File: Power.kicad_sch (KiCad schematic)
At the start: 14 parts, among them J1 Conn_01x01, J2 Conn_01x01, J3 Conn_01x01, J4 Conn_01x01, J5 Conn_01x01, Q1 BSP89, Q2 BSP89, Q3 BSP89, Q4 BSP89, Q5 BSP89, Q6 BSP89

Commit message: Стартовый вариант
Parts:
- added C14, C15, C16, C17, C18, C19, C20, C21, C22, C23, C24, C25, C26, C27, C28, C29, C30, C31, C32, C33, C34, C35, C36, C37, C38, C39, C40, C41, C42, C43, C44, C45, C46, C47, C48: 4.7u, Capacitor_SMD:C_1206_3216Metric_Pad1.33x1.80mm_HandSolder, symbol Device:C_Small
- C3: footprint Capacitor_THT:CP_Axial_L30.0mm_D18.0mm_P35.00mm_Horizontal -> Capacitor_THT:CP_Axial_L18.0mm_D8.0mm_P25.00mm_Horizontal
- J1, J2, J3, J4, J5: footprint (none) -> Connector_My:Power_Wire
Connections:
- net A2 is gone; now on net A: J1.1 (Pin_1)
- net B2 is gone; now on net B: J2.1 (Pin_1)
- net C2 is gone; now on net C: J3.1 (Pin_1)
- net +24V: now also C14.1, C15.1, C16.1, C17.1, C18.1, C19.1, C20.1, C21.1, C22.1, C23.1, C24.1, C25.1, C26.1, C27.1, C28.1, C29.1, C30.1, C31.1, C32.1, C33.1, C34.1, C35.1, C36.1, C37.1, C38.1, C39.1, C40.1, C41.1, C42.1, C43.1, C44.1, C45.1, C46.1, C47.1, C48.1
- net GND: now also C14.2, C15.2, C16.2, C17.2, C18.2, C19.2, C20.2, C21.2, C22.2, C23.2, C24.2, C25.2, C26.2, C27.2, C28.2, C29.2, C30.2, C31.2, C32.2, C33.2, C34.2, C35.2, C36.2, C37.2, C38.2, C39.2, C40.2, C41.2, C42.2, C43.2, C44.2, C45.2, C46.2, C47.2, C48.2
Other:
- moved on the sheet: C1, C2, C3, J1, J2, J3, J4, J5, Q1, Q2, Q3, Q4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

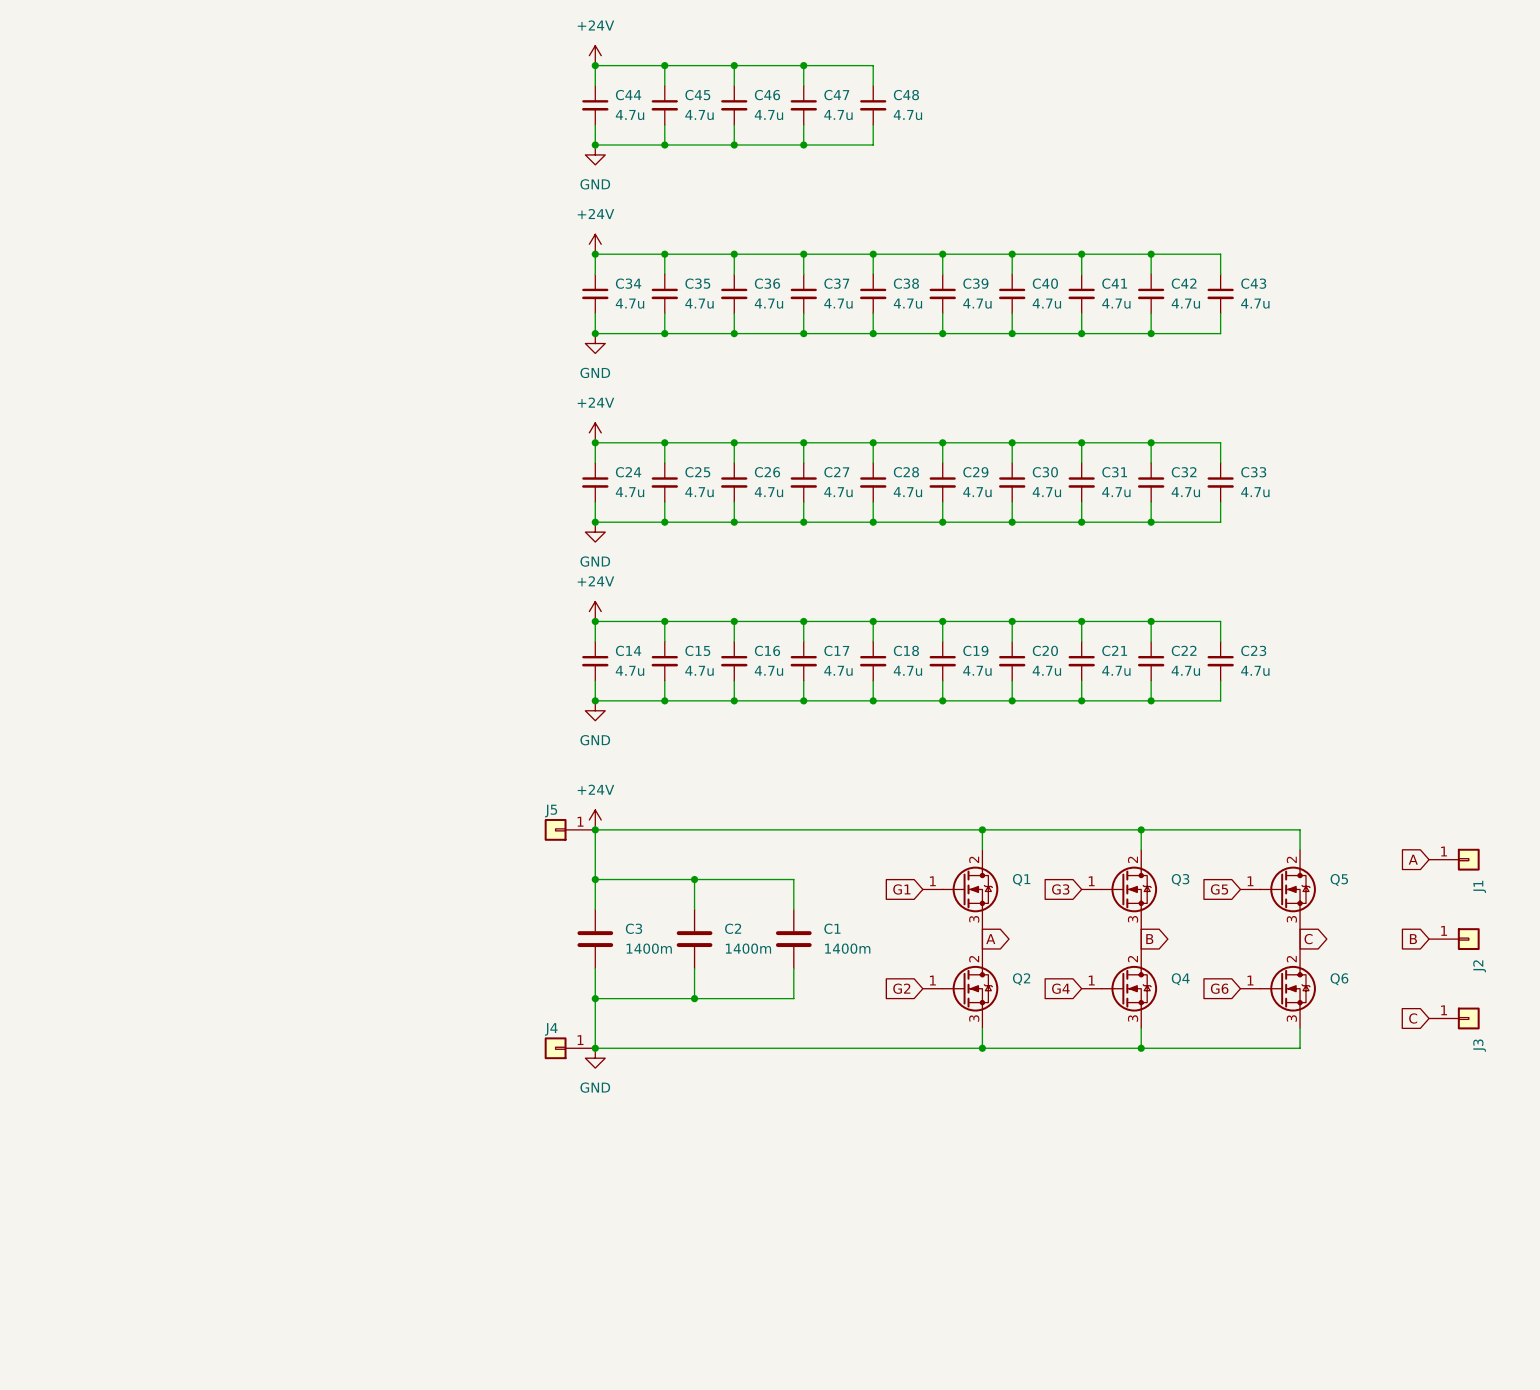
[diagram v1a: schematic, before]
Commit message: Добавил шунты
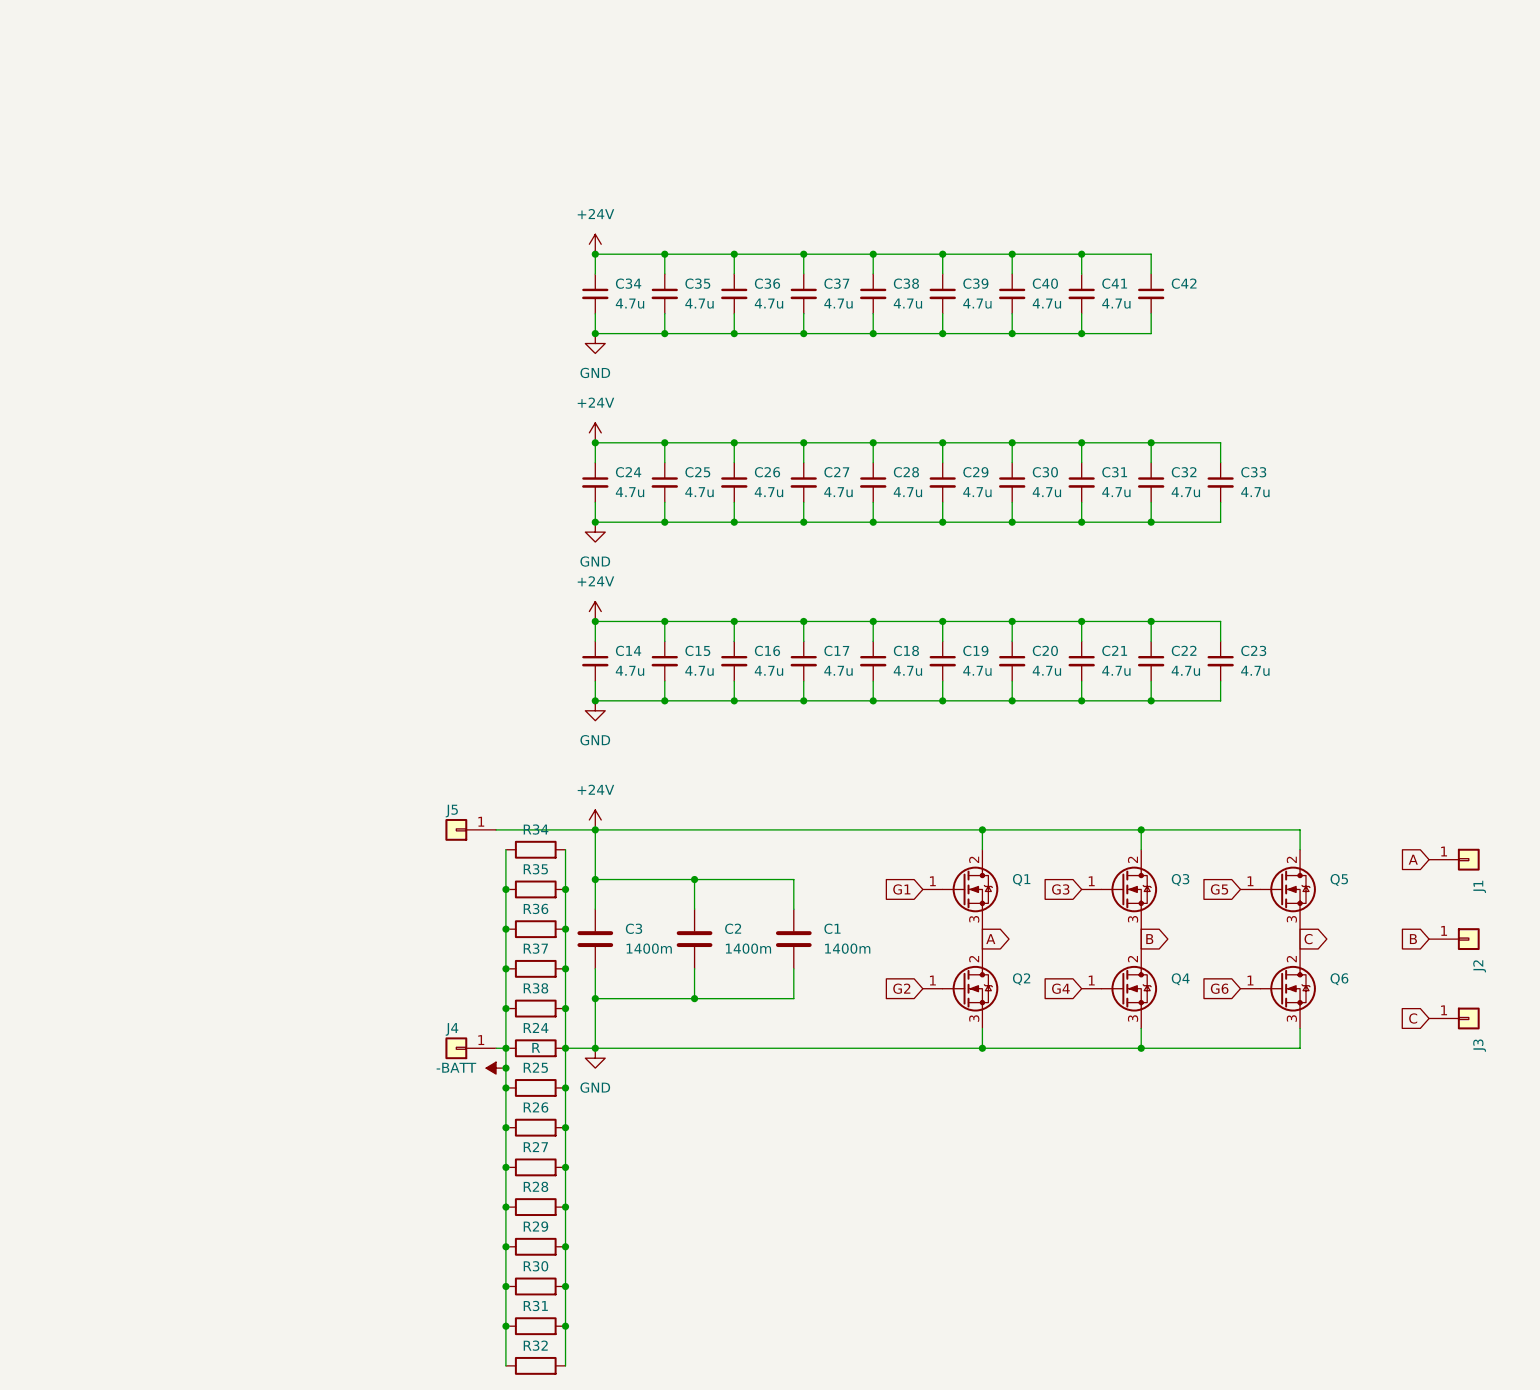
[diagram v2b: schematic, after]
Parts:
- removed C43, C44, C45, C46, C47, C48: 4.7u, Capacitor_SMD:C_1206_3216Metric_Pad1.33x1.80mm_HandSolder, symbol Device:C_Small
- added R24, R25, R26, R27, R28, R29, R30, R31, R32, R34, R35, R36, R37, R38: R, Resistor_SMD:R_2512_6332Metric_Pad1.40x3.35mm_HandSolder, symbol Device:R
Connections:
- net GND: now also R24.2, R25.2, R26.2, R27.2, R28.2, R29.2, R30.2, R31.2, R32.2, R34.2, R35.2, R36.2, R37.2, R38.2; no longer J4.1 (Pin_1)
- new net -BATT: J4.1 (Pin_1), R24.1, R25.1, R26.1, R27.1, R28.1, R29.1, R30.1, R31.1, R32.1, R34.1, R35.1, R36.1, R37.1, R38.1
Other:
- moved on the sheet: J4, J5

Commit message: Для презентации
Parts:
- removed C1: 1400m, Capacitor_THT:CP_Axial_L30.0mm_D18.0mm_P35.00mm_Horizontal, symbol Device:C
- removed R24, R25, R26, R27, R28, R29, R30, R31, R32, R35, R36, R37, R38: R, Resistor_SMD:R_2512_6332Metric_Pad1.40x3.35mm_HandSolder, symbol Device:R
- C3: footprint Capacitor_THT:CP_Axial_L18.0mm_D8.0mm_P25.00mm_Horizontal -> Capacitor_THT:CP_Axial_L30.0mm_D18.0mm_P35.00mm_Horizontal
- R34: footprint Resistor_SMD:R_2512_6332Metric_Pad1.40x3.35mm_HandSolder -> Resistor_SMD:R_Shunt_Vishay_WSR2_WSR3
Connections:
- net +24V: now also R34.1; no longer Q1.2 (D), Q3.2 (D), Q5.2 (D)
- net GND: now also J4.1 (Pin_1); no longer R34.2
- removed net -BATT: J4.1 (Pin_1), R34.1
- new net: Q1.2 (D), Q3.2 (D), Q5.2 (D), R34.2
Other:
- moved on the sheet: R34

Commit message: Стартовый вариант
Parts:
- removed C34, C35, C36, C37, C38, C39, C40, C41, C42: 4.7u, Capacitor_SMD:C_1206_3216Metric_Pad1.33x1.80mm_HandSolder, symbol Device:C_Small
- added R1: R, Shunt_My:TLRS1050, symbol Device:R
- R34: footprint Resistor_SMD:R_Shunt_Vishay_WSR2_WSR3 -> Shunt_My:TLRS1050
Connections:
- net +24V: now also R1.1
- net Shunt_2: now reaches Q1.2 (D), Q3.2 (D), Q5.2 (D), R34.2
- net Shunt_2: now also R1.2

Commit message: Стартовая версия
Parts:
- removed C22, C23, C24, C25, C26, C27, C28, C29, C30, C31, C32, C33: 4.7u, Capacitor_SMD:C_1206_3216Metric_Pad1.33x1.80mm_HandSolder, symbol Device:C_Small

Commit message: Стартовая версия
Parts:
- removed C14, C15, C16, C17, C18, C19, C20, C21: 4.7u, Capacitor_SMD:C_1206_3216Metric_Pad1.33x1.80mm_HandSolder, symbol Device:C_Small
- removed C2: 1400m, Capacitor_THT:CP_Axial_L30.0mm_D18.0mm_P35.00mm_Horizontal, symbol Device:C
- removed Q1, Q2, Q3, Q4, Q5, Q6: BSP89, Package_TO_SOT_SMD:TO-263-2, symbol Transistor_FET:BSP89
- added Q1 (x24): BSP89, Package_SON:VSONP-8-1EP_5x6_P1.27mm, symbol Transistor_FET:BSP89
- C3: footprint Capacitor_THT:CP_Axial_L30.0mm_D18.0mm_P35.00mm_Horizontal -> Capacitor_SMD:CP_Elec_10x12.5
- J4, J5: footprint Connector_My:Power_Wire -> (none)
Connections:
- net A: now also Q1.2 (D), Q1.2 (D), Q1.2 (D), Q1.2 (D), Q1.3 (S), Q1.3 (S), Q1.3 (S), Q1.3 (S)
- net B: now also Q1.2 (D), Q1.2 (D), Q1.2 (D), Q1.2 (D), Q1.3 (S), Q1.3 (S), Q1.3 (S), Q1.3 (S)
- net C: now also Q1.2 (D), Q1.2 (D), Q1.2 (D), Q1.2 (D), Q1.3 (S), Q1.3 (S), Q1.3 (S), Q1.3 (S)
- net G1: now also Q1.1 (G), Q1.1 (G), Q1.1 (G), Q1.1 (G)
- net G2: now also Q1.1 (G), Q1.1 (G), Q1.1 (G), Q1.1 (G)
- net G3: now also Q1.1 (G), Q1.1 (G), Q1.1 (G), Q1.1 (G)
- net G4: now also Q1.1 (G), Q1.1 (G), Q1.1 (G), Q1.1 (G)
- net G5: now also Q1.1 (G), Q1.1 (G), Q1.1 (G), Q1.1 (G)
- net G6: now also Q1.1 (G), Q1.1 (G), Q1.1 (G), Q1.1 (G)
- net GND: now also Q1.3 (S), Q1.3 (S), Q1.3 (S), Q1.3 (S), Q1.3 (S), Q1.3 (S), Q1.3 (S), Q1.3 (S), Q1.3 (S), Q1.3 (S), Q1.3 (S), Q1.3 (S)
- net Shunt_2: now also Q1.2 (D), Q1.2 (D), Q1.2 (D), Q1.2 (D), Q1.2 (D), Q1.2 (D), Q1.2 (D), Q1.2 (D), Q1.2 (D), Q1.2 (D), Q1.2 (D), Q1.2 (D)
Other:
- moved on the sheet: R1, R34

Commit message: Стартовая версия
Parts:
- removed C3: 1400m, Capacitor_SMD:CP_Elec_10x12.5, symbol Device:C
- removed Q1 (x24): BSP89, Package_SON:VSONP-8-1EP_5x6_P1.27mm, symbol Transistor_FET:BSP89
- added C3 (x2): 1500p, Capacitor_THT:C_Rect_L10.0mm_W3.0mm_P7.50mm_FKS3_FKP3, symbol Device:C
- added Q1, Q2, Q3, Q4, Q5, Q6: 2N7002, MOSFET_My:IPTG007N06NM5ATMA1, symbol Transistor_FET:2N7002
- renumbered R34 to R1, R1 to R2
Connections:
- net +24V: now also C3.2
- net A: now also Q1.2 (S), Q2.3 (D)
- net B: now also Q3.2 (S), Q4.3 (D)
- net C: now also Q5.2 (S), Q6.3 (D)
- net G1: now also Q1.1 (G)
- net G2: now also Q2.1 (G)
- net G3: now also Q3.1 (G)
- net G4: now also Q4.1 (G)
- net G5: now also Q5.1 (G)
- net G6: now also Q6.1 (G)
- net GND: now also C3.1, Q2.2 (S), Q4.2 (S), Q6.2 (S)
- net Shunt_2: now also Q1.3 (D), Q3.3 (D), Q5.3 (D)
- new net Earth_Protective: C3.1, C3.2
